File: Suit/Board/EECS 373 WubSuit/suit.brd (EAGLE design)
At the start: 66.4 x 86.1 mm, 56 parts, among them X1 MINI-USB_4P-85-32004-10X

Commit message: More arduino work, added values to some resistors in eagle
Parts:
- R1, R10, R12, R2, R4, R5, R6, R7, R8, R9: value (none) -> 1k
- R13, R14, R3: value (none) -> 10k
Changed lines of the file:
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@@
 <attribute name="VALUE" x="37.592" y="33.8328" size="1.27" layer="27"/>
 </element>
-<element name="R4" library="resistor" package="0207/10" value="" x="36.322" y="10.9728" smashed="yes" rot="R270">
+<element name="R4" library="resistor" package="0207/10" value="1k" x="36.322" y="10.9728" smashed="yes" rot="R270">
 <attribute name="NAME" x="35.306" y="12.7508" size="1.27" layer="25" ratio="10" rot="R270"/>
 <attribute name="VALUE" x="35.687" y="13.2334" size="1.27" layer="27" ratio="10" rot="R270"/>
@@
 </element>
 <element name="Q1" library="special" package="QS" value="" x="15.3924" y="27.813" rot="R180"/>
-<element name="R3" library="resistor" package="0207/10" value="" x="18.542" y="43.9928" rot="R270"/>
-<element name="R5" library="resistor" package="0207/10" value="" x="33.782" y="10.9728" smashed="yes" rot="R270">
+<element name="R3" library="resistor" package="0207/10" value="10k" x="18.542" y="43.9928" rot="R270"/>
+<element name="R5" library="resistor" package="0207/10" value="1k" x="33.782" y="10.9728" smashed="yes" rot="R270">
 <attribute name="NAME" x="32.766" y="12.7508" size="1.27" layer="25" ratio="10" rot="R270"/>
 <attribute name="VALUE" x="33.147" y="13.2334" size="1.27" layer="27" ratio="10" rot="R270"/>
@@
 <attribute name="VALUE" x="31.242" y="22.4028" size="0.6096" layer="27" rot="R270"/>
 </element>
-<element name="R6" library="resistor" package="0207/10" value="" x="31.242" y="10.9728" smashed="yes" rot="R270">
+<element name="R6" library="resistor" package="0207/10" value="1k" x="31.242" y="10.9728" smashed="yes" rot="R270">
 <attribute name="NAME" x="30.226" y="12.7508" size="1.27" layer="25" ratio="10" rot="R270"/>
 <attribute name="VALUE" x="30.607" y="13.2334" size="1.27" layer="27" ratio="10" rot="R270"/>
@@
 <attribute name="VALUE" x="28.702" y="22.4028" size="0.6096" layer="27" rot="R270"/>
 </element>
-<element name="R7" library="resistor" package="0207/10" value="" x="28.702" y="10.9728" smashed="yes" rot="R270">
+<element name="R7" library="resistor" package="0207/10" value="1k" x="28.702" y="10.9728" smashed="yes" rot="R270">
 <attribute name="NAME" x="27.686" y="12.7508" size="1.27" layer="25" ratio="10" rot="R270"/>
 <attribute name="VALUE" x="28.067" y="13.2334" size="1.27" layer="27" ratio="10" rot="R270"/>
@@
 <attribute name="VALUE" x="26.162" y="22.4028" size="0.6096" layer="27" rot="R270"/>
 </element>
-<element name="R8" library="resistor" package="0207/10" value="" x="51.562" y="24.9428" smashed="yes">
+<element name="R8" library="resistor" package="0207/10" value="1k" x="51.562" y="24.9428" smashed="yes">
 <attribute name="NAME" x="49.784" y="23.9268" size="1.27" layer="25" ratio="10"/>
 <attribute name="VALUE" x="49.3014" y="24.3078" size="1.27" layer="27" ratio="10"/>
 </element>
 <element name="C8" library="SparkFun-Passives" package="CAP-PTH-SMALLEZ" value="" x="61.722" y="24.9428" rot="R180"/>
-<element name="R9" library="resistor" package="0207/10" value="" x="51.562" y="27.4828" smashed="yes">
+<element name="R9" library="resistor" package="0207/10" value="1k" x="51.562" y="27.4828" smashed="yes">
 <attribute name="NAME" x="49.784" y="26.4668" size="1.27" layer="25" ratio="10"/>
 <attribute name="VALUE" x="49.3014" y="26.8478" size="1.27" layer="27" ratio="10"/>
 </element>
 <element name="C9" library="SparkFun-Passives" package="CAP-PTH-SMALLEZ" value="" x="61.722" y="27.4828" rot="R180"/>
-<element name="R10" library="resistor" package="0207/10" value="" x="51.562" y="30.0228" smashed="yes">
+<element name="R10" library="resistor" package="0207/10" value="1k" x="51.562" y="30.0228" smashed="yes">
 <attribute name="NAME" x="49.784" y="29.0068" size="1.27" layer="25" ratio="10"/>
 <attribute name="VALUE" x="49.3014" y="29.3878" size="1.27" layer="27" ratio="10"/>
 </element>
 <element name="C10" library="SparkFun-Passives" package="CAP-PTH-SMALLEZ" value="" x="61.722" y="30.0228" rot="R180"/>
-<element name="R12" library="resistor" package="0207/10" value="" x="51.562" y="32.5628" smashed="yes">
+<element name="R12" library="resistor" package="0207/10" value="1k" x="51.562" y="32.5628" smashed="yes">
 <attribute name="NAME" x="49.784" y="31.5468" size="1.27" layer="25" ratio="10"/>
 <attribute name="VALUE" x="49.3014" y="31.9278" size="1.27" layer="27" ratio="10"/>
@@
 <attribute name="NAME" x="52.705" y="17.0688" size="1.27" layer="25" ratio="10" rot="R180"/>
 </element>
-<element name="R1" library="resistor" package="0207/10" value="" x="24.892" y="14.7828" smashed="yes" rot="R90">
+<element name="R1" library="resistor" package="0207/10" value="1k" x="24.892" y="14.7828" smashed="yes" rot="R90">
 <attribute name="NAME" x="25.908" y="13.0048" size="1.27" layer="25" ratio="10" rot="R90"/>
 <attribute name="VALUE" x="25.527" y="12.5222" size="1.27" layer="27" ratio="10" rot="R90"/>
 </element>
-<element name="R2" library="resistor" package="0207/10" value="" x="22.352" y="14.7828" smashed="yes" rot="R90">
+<element name="R2" library="resistor" package="0207/10" value="1k" x="22.352" y="14.7828" smashed="yes" rot="R90">
 <attribute name="NAME" x="23.368" y="13.0048" size="1.27" layer="25" ratio="10" rot="R90"/>
 <attribute name="VALUE" x="22.987" y="12.5222" size="1.27" layer="27" ratio="10" rot="R90"/>
@@
 <attribute name="VALUE" x="38.227" y="68.4022" size="1.27" layer="27" ratio="10" rot="R90"/>
 </element>
-<element name="R13" library="resistor" package="0207/10" value="" x="31.242" y="70.6628" smashed="yes" rot="R90">
+<element name="R13" library="resistor" package="0207/10" value="10k" x="31.242" y="70.6628" smashed="yes" rot="R90">
 <attribute name="NAME" x="31.8262" y="68.9356" size="1.27" layer="25" ratio="10" rot="R90"/>
 <attribute name="VALUE" x="31.877" y="68.4022" size="1.27" layer="27" ratio="10" rot="R90"/>
 </element>
-<element name="R14" library="resistor" package="0207/10" value="" x="24.892" y="70.6628" smashed="yes" rot="R90">
+<element name="R14" library="resistor" package="0207/10" value="10k" x="24.892" y="70.6628" smashed="yes" rot="R90">
 <attribute name="NAME" x="25.4762" y="68.9102" size="1.27" layer="25" ratio="10" rot="R90"/>
 <attribute name="VALUE" x="25.527" y="68.4022" size="1.27" layer="27" ratio="10" rot="R90"/>

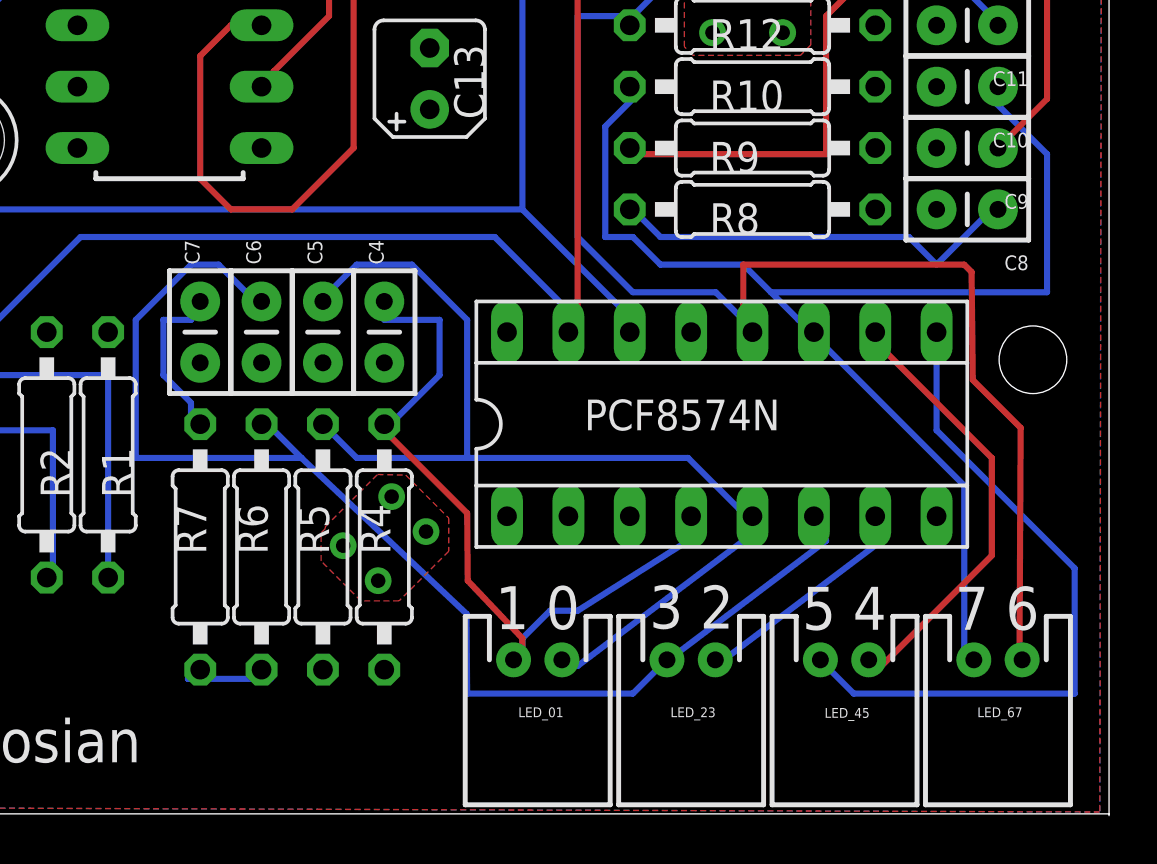
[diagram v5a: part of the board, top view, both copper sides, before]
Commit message: finished arduino code, fixed PCB error
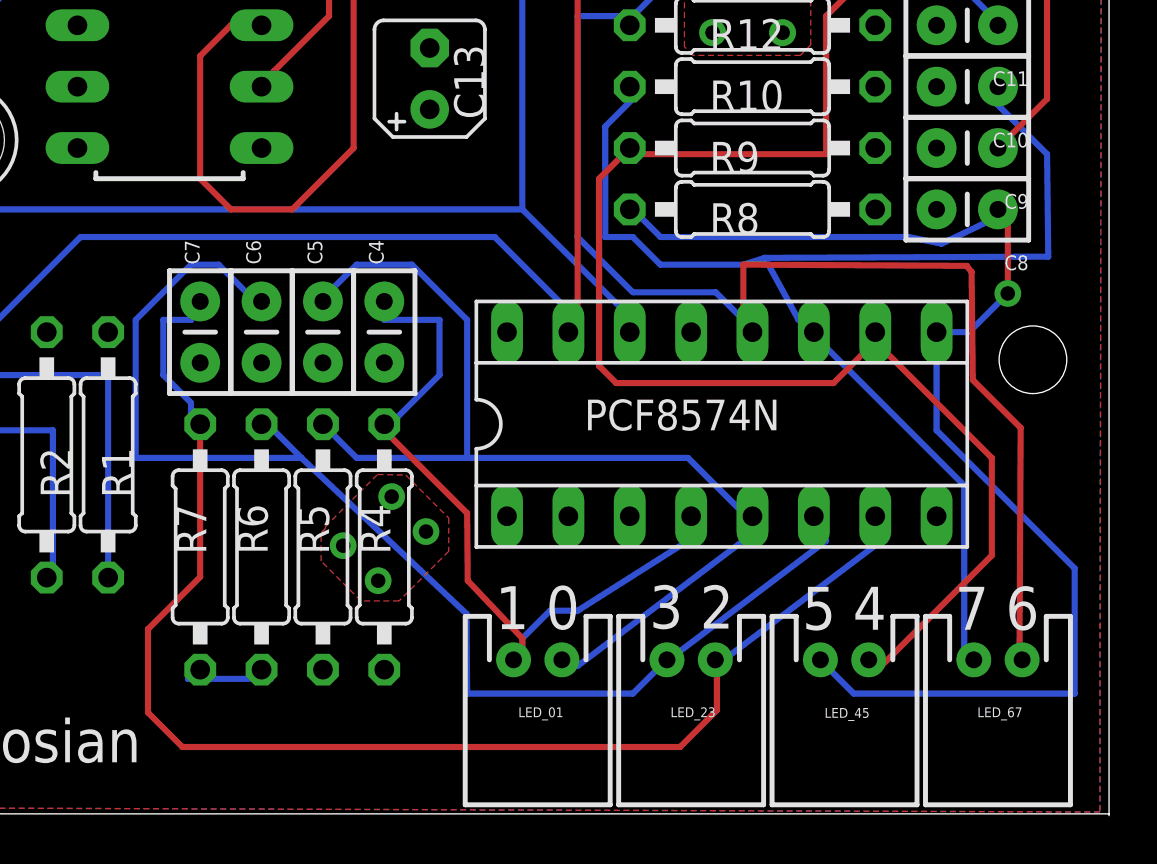
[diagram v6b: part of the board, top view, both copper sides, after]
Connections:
- removed net N$7: C7.1, R7.1
- removed net N$8: C8.1, R8.1
- removed net N$9: C9.1, R9.1
- net LED_3: now also C7.1, R7.1
- net LED_4: now also C8.1, R8.1
- net LED_5: now also C9.1, R9.1
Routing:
- net LED_5: track 18.2 -> 73.6 mm
- net LED_3: track 9.90 -> 57.1 mm
- net N$9: track 33.0 -> 0.00 mm
- net LED_4: track 28.4 -> 52.0 mm, vias 0 -> 1
- net N$8: track 17.1 -> 0.00 mm
- net N$7: track 7.50 -> 0.00 mm
- net LED_6: track 54.7 -> 54.2 mm
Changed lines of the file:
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@@
 <?xml version="1.0" encoding="utf-8"?>
 <!DOCTYPE eagle SYSTEM "eagle.dtd">
-<eagle version="6.3">
+<eagle version="6.5.0">
 <drawing>
 <settings>
@@
 EECS 373
 FA 2013</text>
-<dimension x1="0.0762" y1="-0.0762" x2="66.3194" y2="-0.1524" x3="33.18578125" y3="-10.5635625" layer="25"/>
-<dimension x1="66.3194" y1="-0.0762" x2="66.3194" y2="85.979" x3="82.9056" y3="42.9514" layer="25"/>
+<dimension x1="0.0762" y1="-0.0762" x2="66.3194" y2="-0.1524" x3="33.18578125" y3="-10.5635625" textsize="3.5" layer="25"/>
+<dimension x1="66.3194" y1="-0.0762" x2="66.3194" y2="85.979" x3="82.9056" y3="42.9514" textsize="3.5" layer="25"/>
 </plain>
 <attributes>
@@
 <wire x1="46.609" y1="32.9438" x2="44.323" y2="32.9438" width="0.254" layer="16"/>
 <wire x1="51.181" y1="20.3708" x2="51.562" y2="19.8628" width="0.254" layer="16"/>
-<wire x1="51.181" y1="22.6568" x2="60.325" y2="22.6568" width="0.254" layer="1"/>
+<wire x1="51.181" y1="22.6568" x2="60.4266" y2="22.606" width="0.254" layer="1"/>
 <wire x1="51.181" y1="20.3708" x2="51.181" y2="22.6568" width="0.254" layer="1"/>
 <wire x1="62.611" y1="6.0452" x2="62.722" y2="6.2992" width="0.254" layer="1"/>
@@
 <wire x1="62.6618" y1="15.9004" x2="60.6806" y2="17.8816" width="0.254" layer="1"/>
 <wire x1="60.6806" y1="17.8816" x2="60.6298" y2="22.352" width="0.254" layer="1"/>
-<wire x1="60.6298" y1="22.352" x2="60.325" y2="22.6568" width="0.254" layer="1"/>
+<wire x1="60.6298" y1="22.352" x2="60.4266" y2="22.606" width="0.254" layer="1"/>
 </signal>
 <signal name="VCC">
@@
 <wire x1="56.896" y1="11.2268" x2="56.642" y2="12.2428" width="0.254" layer="16"/>
 <wire x1="50.038" y1="6.0452" x2="50.022" y2="6.2992" width="0.254" layer="16"/>
+<contactref element="C7" pad="1"/>
+<contactref element="R7" pad="1"/>
+<wire x1="28.321" y1="16.9418" x2="28.321" y2="15.7988" width="0.254" layer="16"/>
+<wire x1="27.178" y1="18.0848" x2="28.321" y2="16.9418" width="0.254" layer="16"/>
+<wire x1="27.178" y1="20.3708" x2="27.178" y2="18.0848" width="0.254" layer="16"/>
+<wire x1="28.321" y1="20.3708" x2="27.178" y2="20.3708" width="0.254" layer="16"/>
+<wire x1="28.321" y1="15.7988" x2="28.702" y2="16.0528" width="0.254" layer="16"/>
+<wire x1="28.321" y1="20.3708" x2="28.702" y2="21.1328" width="0.254" layer="16"/>
+<wire x1="28.702" y1="16.0528" x2="28.702" y2="9.7282" width="0.254" layer="1"/>
+<wire x1="28.702" y1="9.7282" x2="26.543" y2="7.5692" width="0.254" layer="1"/>
+<wire x1="26.543" y1="7.5692" x2="26.543" y2="4.1148" width="0.254" layer="1"/>
+<wire x1="26.543" y1="4.1148" x2="27.9654" y2="2.6924" width="0.254" layer="1"/>
+<wire x1="27.9654" y1="2.6924" x2="48.5648" y2="2.6924" width="0.254" layer="1"/>
+<wire x1="48.5648" y1="2.6924" x2="50.0888" y2="4.2164" width="0.254" layer="1"/>
+<wire x1="50.0888" y1="4.2164" x2="50.0888" y2="6.2324" width="0.254" layer="1"/>
+<wire x1="50.0888" y1="6.2324" x2="50.022" y2="6.2992" width="0.254" layer="1"/>
 </signal>
 <signal name="LED_4">
@@
 <wire x1="54.61" y1="6.0452" x2="55.753" y2="4.9022" width="0.254" layer="16"/>
 <wire x1="54.61" y1="6.0452" x2="54.372" y2="6.2992" width="0.254" layer="16"/>
+<contactref element="C8" pad="1"/>
+<contactref element="R8" pad="1"/>
+<wire x1="47.752" y1="23.7998" x2="46.609" y2="24.9428" width="0.254" layer="16"/>
+<wire x1="58.039" y1="23.7998" x2="47.752" y2="23.7998" width="0.254" layer="16"/>
+<wire x1="59.3852" y1="23.5204" x2="58.039" y2="23.7998" width="0.254" layer="16"/>
+<wire x1="61.722" y1="24.638" x2="59.3852" y2="23.5204" width="0.254" layer="16"/>
+<wire x1="46.609" y1="24.9428" x2="46.482" y2="24.9428" width="0.254" layer="16"/>
+<wire x1="61.722" y1="24.638" x2="61.722" y2="24.9428" width="0.254" layer="16"/>
+<via x="62.1284" y="21.463" extent="1-16" drill="0.6"/>
+<wire x1="59.182" y1="19.8628" x2="60.5282" y2="19.8628" width="0.254" layer="16"/>
+<wire x1="60.5282" y1="19.8628" x2="62.1284" y2="21.463" width="0.254" layer="16"/>
+<wire x1="62.1284" y1="21.463" x2="62.1284" y2="24.5364" width="0.254" layer="1"/>
+<wire x1="62.1284" y1="24.5364" x2="61.722" y2="24.9428" width="0.254" layer="1"/>
 </signal>
 <signal name="LED_5">
@@
 <wire x1="56.896" y1="19.2278" x2="56.642" y2="19.8628" width="0.254" layer="1"/>
 <wire x1="56.896" y1="6.0452" x2="56.372" y2="6.2992" width="0.254" layer="1"/>
+<contactref element="C9" pad="1"/>
+<contactref element="R9" pad="1"/>
+<wire x1="54.61" y1="27.2288" x2="46.609" y2="27.2288" width="0.254" layer="1"/>
+<wire x1="54.61" y1="32.9438" x2="54.61" y2="27.2288" width="0.254" layer="1"/>
+<wire x1="56.896" y1="35.2298" x2="54.61" y2="32.9438" width="0.254" layer="1"/>
+<wire x1="63.754" y1="35.2298" x2="56.896" y2="35.2298" width="0.254" layer="1"/>
+<wire x1="63.754" y1="29.5148" x2="63.754" y2="35.2298" width="0.254" layer="1"/>
+<wire x1="61.722" y1="27.4828" x2="63.754" y2="29.5148" width="0.254" layer="1"/>
+<wire x1="46.609" y1="27.2288" x2="46.482" y2="27.4828" width="0.254" layer="1"/>
+<wire x1="61.468" y1="27.2288" x2="61.722" y2="27.4828" width="0.254" layer="1"/>
+<wire x1="56.642" y1="19.8628" x2="56.642" y2="19.4818" width="0.254" layer="1"/>
+<wire x1="56.642" y1="19.4818" x2="54.9148" y2="17.7546" width="0.254" layer="1"/>
+<wire x1="54.9148" y1="17.7546" x2="45.9232" y2="17.7546" width="0.254" layer="1"/>
+<wire x1="45.9232" y1="17.7546" x2="45.212" y2="18.4658" width="0.254" layer="1"/>
+<wire x1="45.212" y1="18.4658" x2="45.212" y2="26.2128" width="0.254" layer="1"/>
+<wire x1="45.212" y1="26.2128" x2="46.482" y2="27.4828" width="0.254" layer="1"/>
 </signal>
 <signal name="LED_6">
@@
 <wire x1="47.752" y1="22.6568" x2="46.609" y2="23.7998" width="0.254" layer="16"/>
 <wire x1="51.181" y1="22.6568" x2="47.752" y2="22.6568" width="0.254" layer="16"/>
-<wire x1="53.467" y1="20.3708" x2="52.324" y2="21.5138" width="0.254" layer="16"/>
-<wire x1="52.324" y1="21.5138" x2="51.181" y2="22.6568" width="0.254" layer="16"/>
+<wire x1="53.467" y1="20.3708" x2="52.07" y2="22.9362" width="0.254" layer="16"/>
+<wire x1="52.07" y1="22.9362" x2="51.181" y2="22.6568" width="0.254" layer="16"/>
 <wire x1="46.609" y1="29.5148" x2="46.482" y2="30.0228" width="0.254" layer="16"/>
 <wire x1="53.467" y1="20.3708" x2="54.102" y2="19.8628" width="0.254" layer="16"/>
 <wire x1="63.754" y1="27.2288" x2="61.468" y2="29.5148" width="0.254" layer="16"/>
-<wire x1="63.754" y1="21.5138" x2="63.754" y2="27.2288" width="0.254" layer="16"/>
-<wire x1="52.324" y1="21.5138" x2="63.754" y2="21.5138" width="0.254" layer="16"/>
+<wire x1="63.8048" y1="22.987" x2="63.754" y2="27.2288" width="0.254" layer="16"/>
+<wire x1="52.07" y1="22.9362" x2="63.8048" y2="22.987" width="0.254" layer="16"/>
 <wire x1="61.468" y1="29.5148" x2="61.722" y2="30.0228" width="0.254" layer="16"/>
 </signal>
@@
 <wire x1="44.323" y1="66.0908" x2="43.942" y2="65.5828" width="0.254" layer="16"/>
 </signal>
-<signal name="N$7">
-<contactref element="C7" pad="1"/>
-<contactref element="R7" pad="1"/>
-<wire x1="28.321" y1="16.9418" x2="28.321" y2="15.7988" width="0.254" layer="16"/>
-<wire x1="27.178" y1="18.0848" x2="28.321" y2="16.9418" width="0.254" layer="16"/>
-<wire x1="27.178" y1="20.3708" x2="27.178" y2="18.0848" width="0.254" layer="16"/>
-<wire x1="28.321" y1="20.3708" x2="27.178" y2="20.3708" width="0.254" layer="16"/>
-<wire x1="28.321" y1="15.7988" x2="28.702" y2="16.0528" width="0.254" layer="16"/>
-<wire x1="28.321" y1="20.3708" x2="28.702" y2="21.1328" width="0.254" layer="16"/>
-</signal>
-<signal name="N$8">
-<contactref element="C8" pad="1"/>
-<contactref element="R8" pad="1"/>
-<wire x1="47.752" y1="23.7998" x2="46.609" y2="24.9428" width="0.254" layer="16"/>
-<wire x1="58.039" y1="23.7998" x2="47.752" y2="23.7998" width="0.254" layer="16"/>
-<wire x1="59.182" y1="22.6568" x2="58.039" y2="23.7998" width="0.254" layer="16"/>
-<wire x1="61.468" y1="24.9428" x2="59.182" y2="22.6568" width="0.254" layer="16"/>
-<wire x1="46.609" y1="24.9428" x2="46.482" y2="24.9428" width="0.254" layer="16"/>
-<wire x1="61.468" y1="24.9428" x2="61.722" y2="24.9428" width="0.254" layer="16"/>
-</signal>
-<signal name="N$9">
-<contactref element="C9" pad="1"/>
-<contactref element="R9" pad="1"/>
-<wire x1="54.61" y1="27.2288" x2="46.609" y2="27.2288" width="0.254" layer="1"/>
-<wire x1="54.61" y1="32.9438" x2="54.61" y2="27.2288" width="0.254" layer="1"/>
-<wire x1="56.896" y1="35.2298" x2="54.61" y2="32.9438" width="0.254" layer="1"/>
-<wire x1="63.754" y1="35.2298" x2="56.896" y2="35.2298" width="0.254" layer="1"/>
-<wire x1="63.754" y1="29.5148" x2="63.754" y2="35.2298" width="0.254" layer="1"/>
-<wire x1="61.722" y1="27.4828" x2="63.754" y2="29.5148" width="0.254" layer="1"/>
-<wire x1="46.609" y1="27.2288" x2="46.482" y2="27.4828" width="0.254" layer="1"/>
-<wire x1="61.468" y1="27.2288" x2="61.722" y2="27.4828" width="0.254" layer="1"/>
-</signal>
 <signal name="N$1">
